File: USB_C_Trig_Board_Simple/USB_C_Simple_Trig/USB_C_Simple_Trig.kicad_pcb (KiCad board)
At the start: 2 copper layers, 43.5 x 46.5 mm, 49 parts, among them IC1 AP33772SDKZ-13-FA01, J1 USB_C_Receptacle, J2 Screw_Terminal_01x04, J3 Conn_01x06_Pin, J4 Conn_ARM_JTAG_SWD_10, Q1 BUK7880-55A/CUX, Q2 BUK7880-55A/CUX, SW1 SW_Push, U10 AP2127N-3.3, U5 STM32C011F6Px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

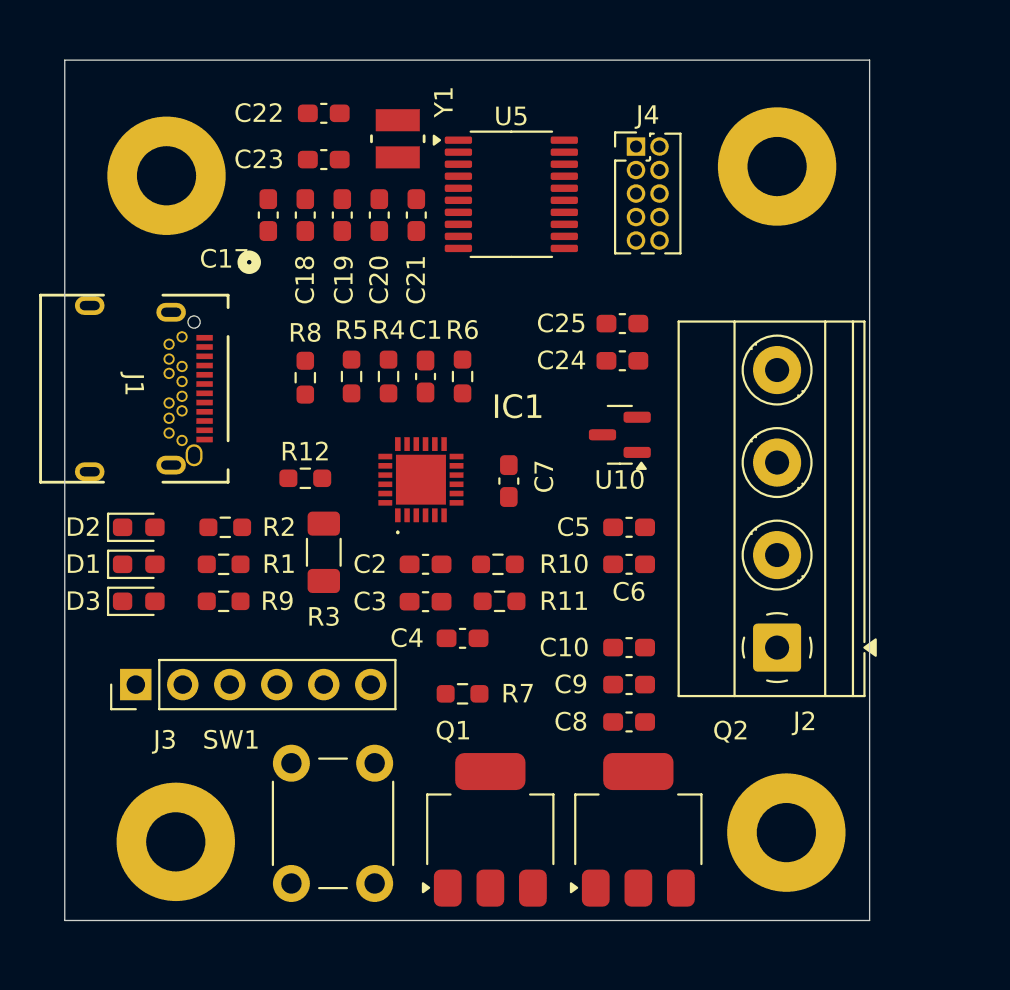
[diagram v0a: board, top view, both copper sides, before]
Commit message: Simple trigger board: finished draft PCB routing
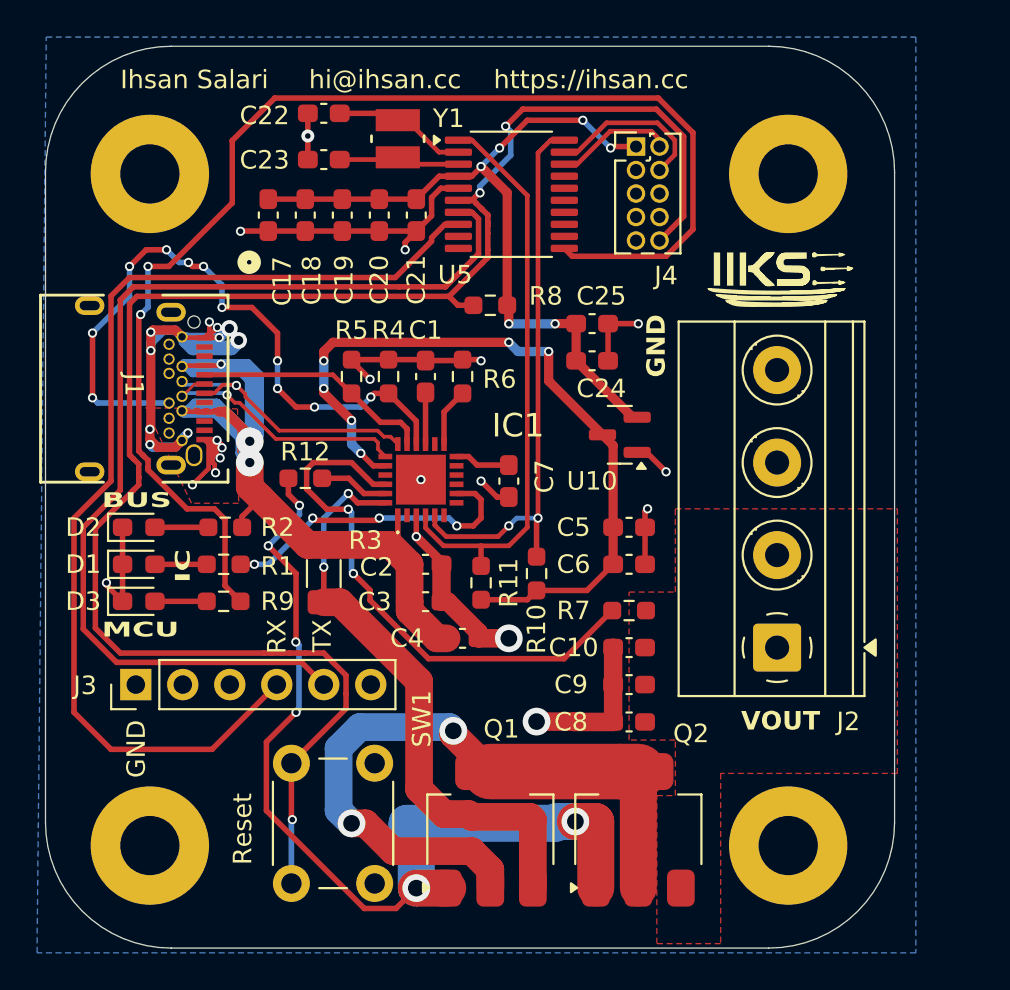
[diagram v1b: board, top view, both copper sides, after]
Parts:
- moved R8 10.7 mm to (141.5, 96.5), turned to 180 degrees
- moved R7 10.1 mm to (149.0, 113.0)
- moved R10 2.15 mm to (144.0, 111.0), turned to 90 degrees
- moved C24 1.64 mm to (147.0, 99.5), turned to 0 degrees
- moved C25 1.64 mm to (147.0, 97.5), turned to 0 degrees
- moved H4 1.41 mm to (123.1, 125.7)
- moved R11 1.41 mm to (141.0, 111.5), turned to 90 degrees
- moved R3 1.15 mm to (132.5, 111.0), turned to -90 degrees
- moved H3 0.91 mm to (123.1, 89.4)
- moved H1 0.72 mm to (157.6, 89.4)
- moved H2 0.71 mm to (157.6, 125.7)
- turned R1 to 0 degrees
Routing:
- net /MCU/NRST: track 0.00 -> 94.5 mm, vias 0 -> 3
- net GND: track 0.00 -> 92.9 mm, vias 0 -> 29
- net /MCU/STATUS_LED: track 0.00 -> 70.4 mm, vias 0 -> 2
- net /MCU/UART_RX: track 0.00 -> 57.1 mm
- net VBUS: track 0.00 -> 56.5 mm, vias 0 -> 3
- net /MCU/UART_TX: track 0.00 -> 56.4 mm
- net Net-(Q1-G): track 0.00 -> 50.3 mm, vias 0 -> 6
- net +3V3: track 0.00 -> 41.7 mm, vias 0 -> 6
- net +5V: track 0.00 -> 41.4 mm, vias 0 -> 6
- net Net-(Q1-D): track 0.00 -> 38.4 mm, vias 0 -> 2
- net /USB_C_IC/CC2: track 0.00 -> 36.2 mm, vias 0 -> 11
- net Net-(IC1-VCC): track 0.00 -> 31.9 mm, vias 0 -> 2
- net /MCU/I2C_SDA: track 0.00 -> 31.0 mm
- net /MCU/I2C_SCL: track 0.00 -> 30.3 mm, vias 0 -> 2
- net Net-(IC1-VOUT): track 0.00 -> 29.5 mm, vias 0 -> 2
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- added copper zone on B.Cu, net GND
- added copper zone on F.Cu, net GND
- added copper zone on F.Cu, net VOUT
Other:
- board size 43.5 x 46.5 mm -> 45.9 x 48.7 mm
- board text added: "BUS"
- board text added: "GND"
- board text added: "IC"
- board text added: "IIKS Technologies"
- board text added: "Ihsan Salari hi@ihsan.cc https://ihsan.cc"
- board text added: "MCU"
- board text added: "RX"
- board text added: "Reset"
- board text added: "TX"
- board text added: "USB-C PD Simple Trigger Board V1.0 Up to 28V 5A with PD EPR PD PPS compatible hi@ihsan.cc"
- board text added: "VOUT"
- board text added: "whoami@ihsan.wtf"

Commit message: Simple  2-Layer Trig:
Rerouted power traces and added some high current copper pour on ground plane.
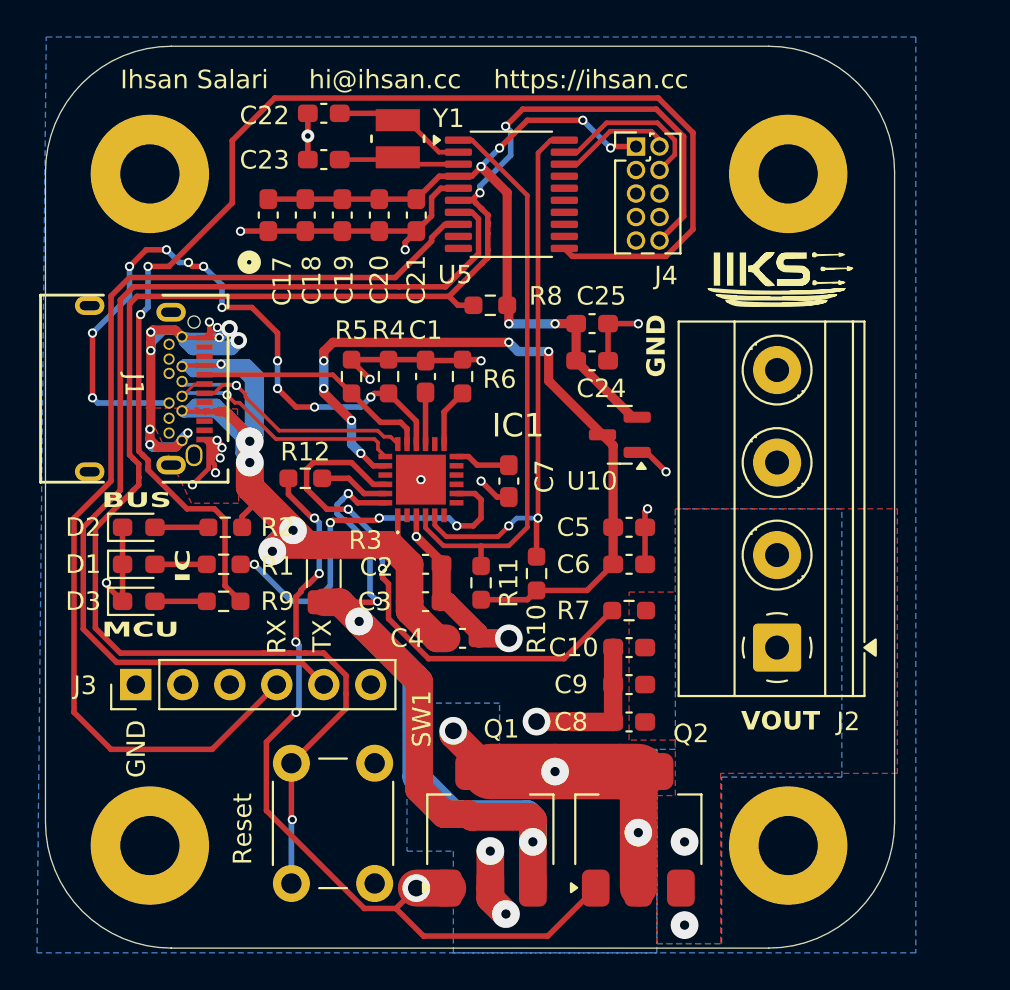
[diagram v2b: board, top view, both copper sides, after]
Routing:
- net Net-(IC1-VCC): track 31.9 -> 53.6 mm, vias 2 -> 4
- net Net-(Q1-D): track 38.4 -> 21.5 mm, vias 2 -> 5
- net VBUS: track 56.5 -> 65.7 mm, vias 3 -> 5
- net Net-(Q1-G): track 50.3 -> 45.0 mm, vias 6 -> 5
- net Net-(IC1-LED): track 17.0 -> 20.5 mm
- net VOUT: vias 0 -> 2
- added copper zone on B.Cu, net Net-(Q1-D)
- added copper zone on B.Cu, net VOUT
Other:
- board text added: "THIS IS THE OG SIMPLE TRIGGER BOARD"

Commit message: Silkscreen update for both simple trig boards.
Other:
- board text added: "USB-C PD Simple Trigger Board V1.0 Up to 28V 5A with PD EPR PD PPS compatible 2-layer board hi@ihsan.cc"
- board text removed: "USB-C PD Simple Trigger Board V1.0 Up to 28V 5A with PD EPR PD PPS compatible hi@ihsan.cc"
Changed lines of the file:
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@@
 		)
 	)
-	(gr_text "USB-C PD Simple Trigger Board V1.0\nUp to 28V 5A with PD EPR\nPD PPS compatible\n\nhi@ihsan.cc\n"
-		(at 130.65 84.55 270)
+	(gr_text "USB-C PD Simple Trigger Board V1.0\nUp to 28V 5A with PD EPR\nPD PPS compatible\n2-layer board\n\nhi@ihsan.cc\n"
+		(at 129.5 84.55 270)
 		(layer "B.SilkS")
 		(effects
